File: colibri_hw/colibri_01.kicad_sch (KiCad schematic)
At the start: 11 parts

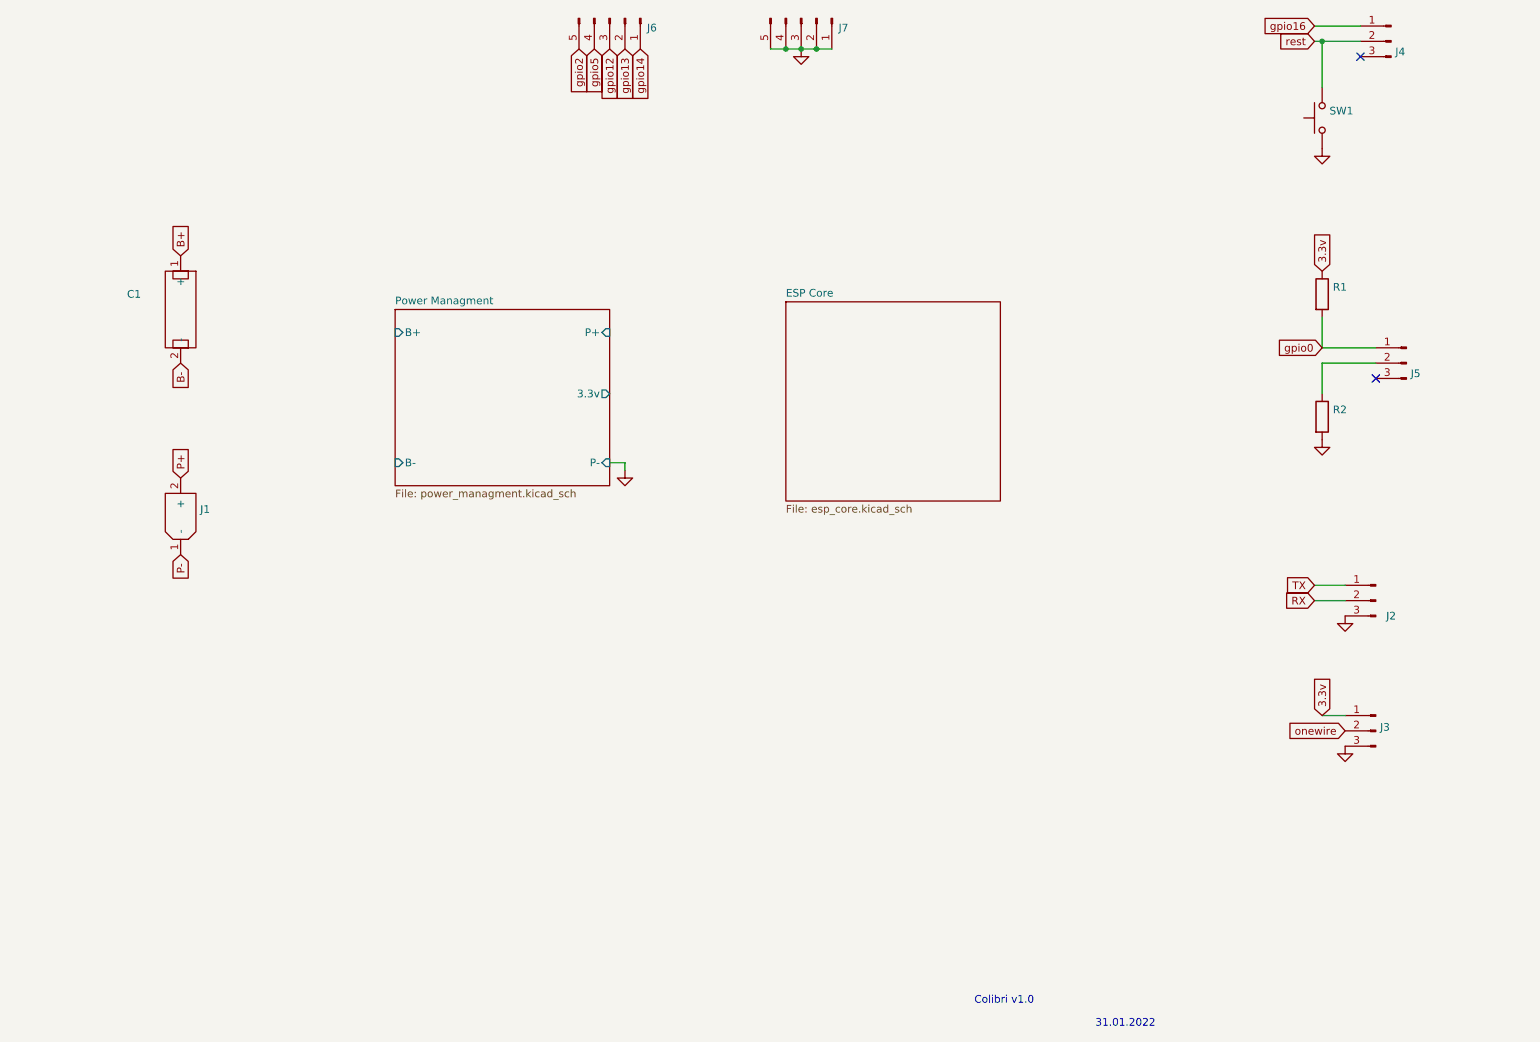
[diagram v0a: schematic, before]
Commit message: [v1.0.1]: Fix UART communication issues due to R5 value
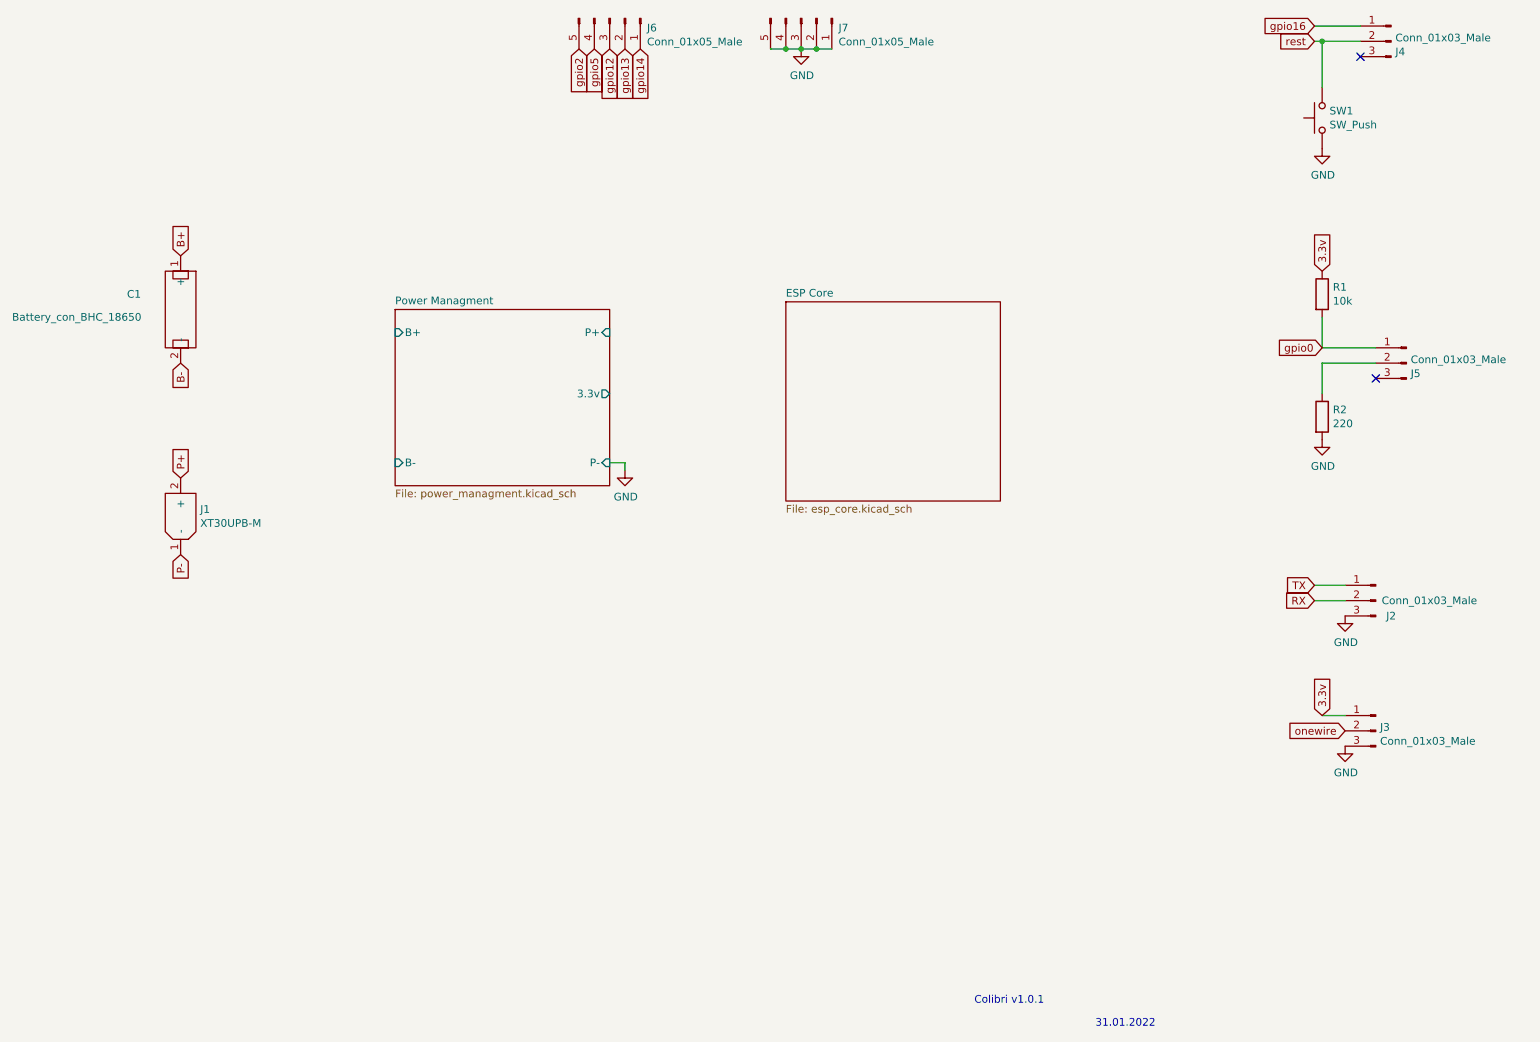
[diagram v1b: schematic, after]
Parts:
- C1: value (none) -> Battery_con_BHC_18650; footprint (none) -> Connector:Battery_con_BHC_18650
- J1: value (none) -> XT30UPB-M; footprint (none) -> XT_con:AMASS_XT30UPB-M_1x02_P5.0mm_Vertical
- J2, J3, J4, J5: value (none) -> Conn_01x03_Male; footprint (none) -> Connector_PinHeader_2.54mm:PinHeader_1x03_P2.54mm_Vertical
- J6, J7: value (none) -> Conn_01x05_Male; footprint (none) -> Connector_PinHeader_2.54mm:PinHeader_1x05_P2.54mm_Vertical
- R1: value (none) -> 10k; footprint (none) -> Resistor_SMD:R_0805_2012Metric
- R2: value (none) -> 220; footprint (none) -> Resistor_SMD:R_0805_2012Metric
- SW1: value (none) -> SW_Push; footprint (none) -> Button_Switch_SMD:TP-1163s
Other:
- note added: "Colibri v1.0.1"
- note removed: "Colibri v1.0"
